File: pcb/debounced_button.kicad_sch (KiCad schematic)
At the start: 5 parts, among them SW3 SW_Push

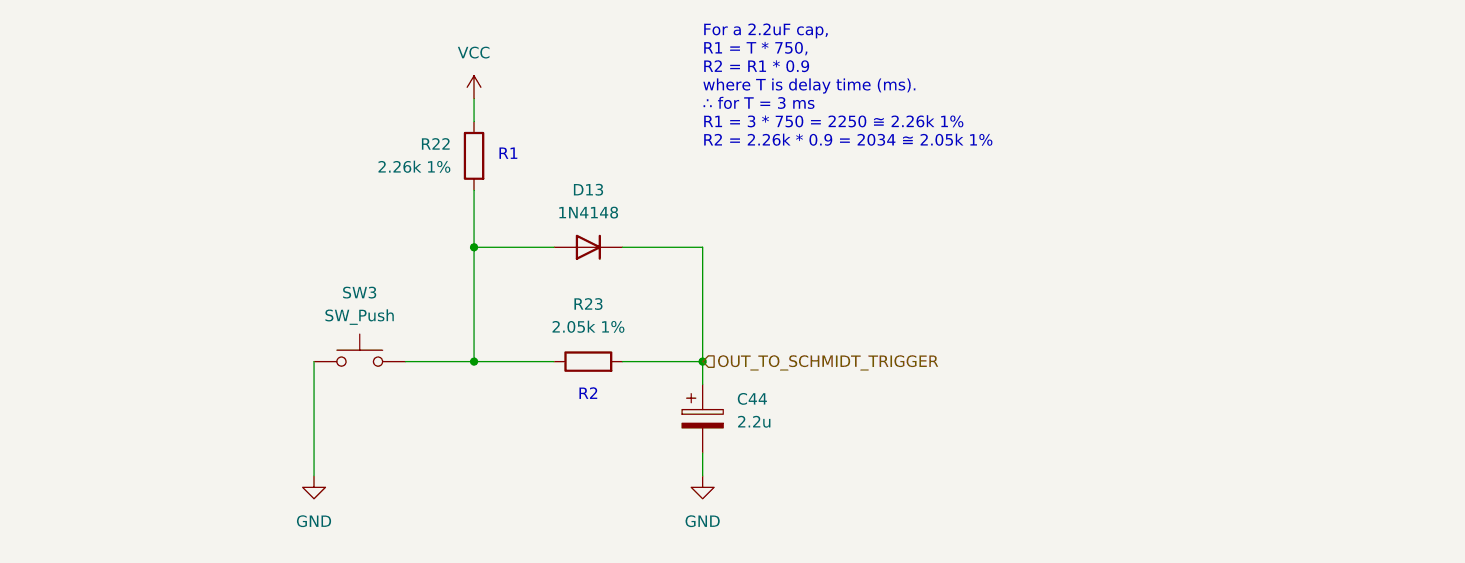
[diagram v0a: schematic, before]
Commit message: expand usb, piano keys, cleanup
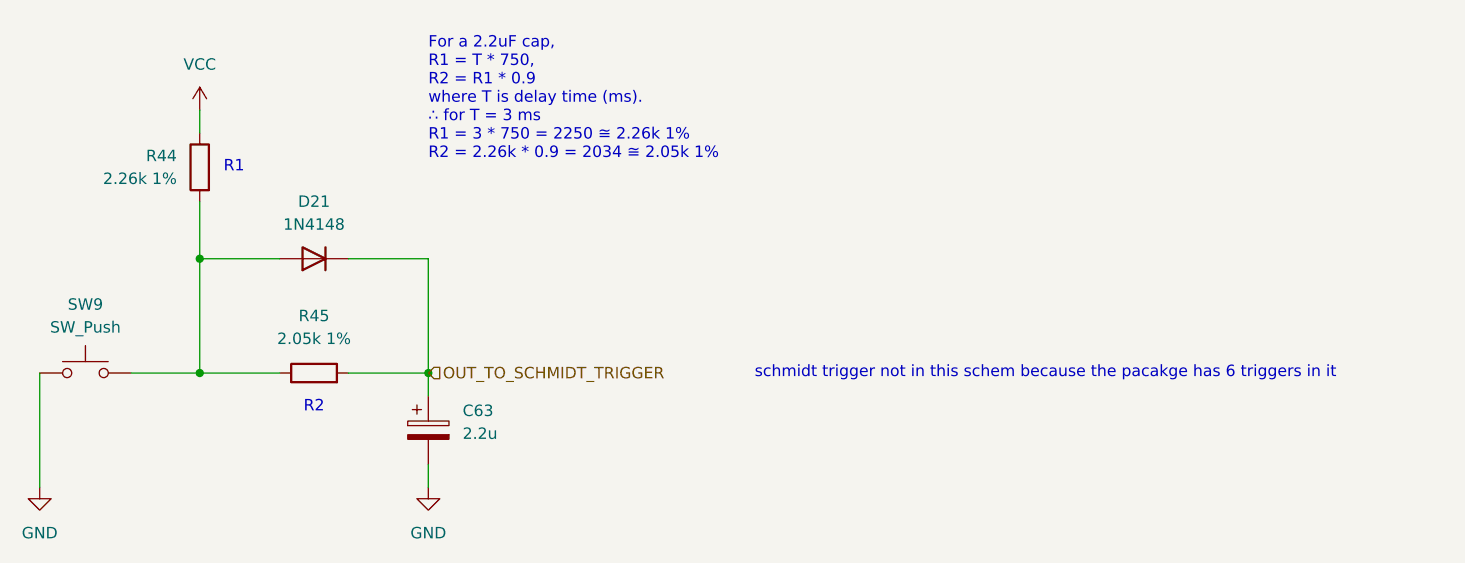
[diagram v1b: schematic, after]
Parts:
- renumbered C44 to C63, D13 to D21, R22 to R44, R23 to R45, SW3 to SW9
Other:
- note added: "schmidt trigger not in this schem because the pacakge has 6 triggers in it"
- moved on the sheet: C63, D21, R44, R45, SW9

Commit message: switch back to rp2350, ideal diode OR'ing for power
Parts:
- renumbered C63 to C53, D21 to D15, R44 to R30, R45 to R31, SW9 to SW3
